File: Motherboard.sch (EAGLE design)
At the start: 8 parts

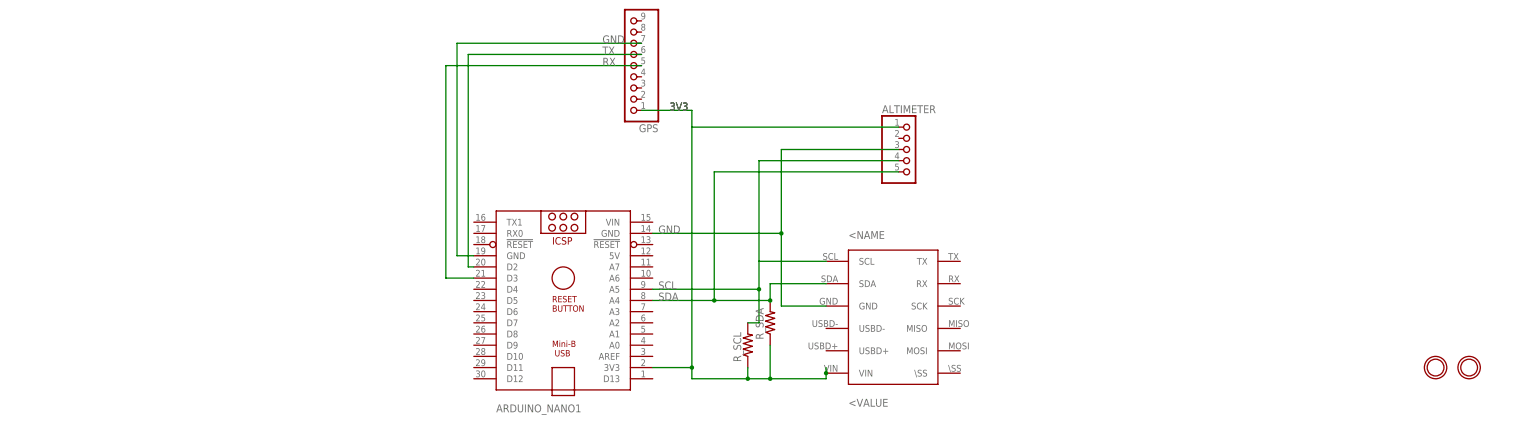
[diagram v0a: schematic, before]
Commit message: add buck converter
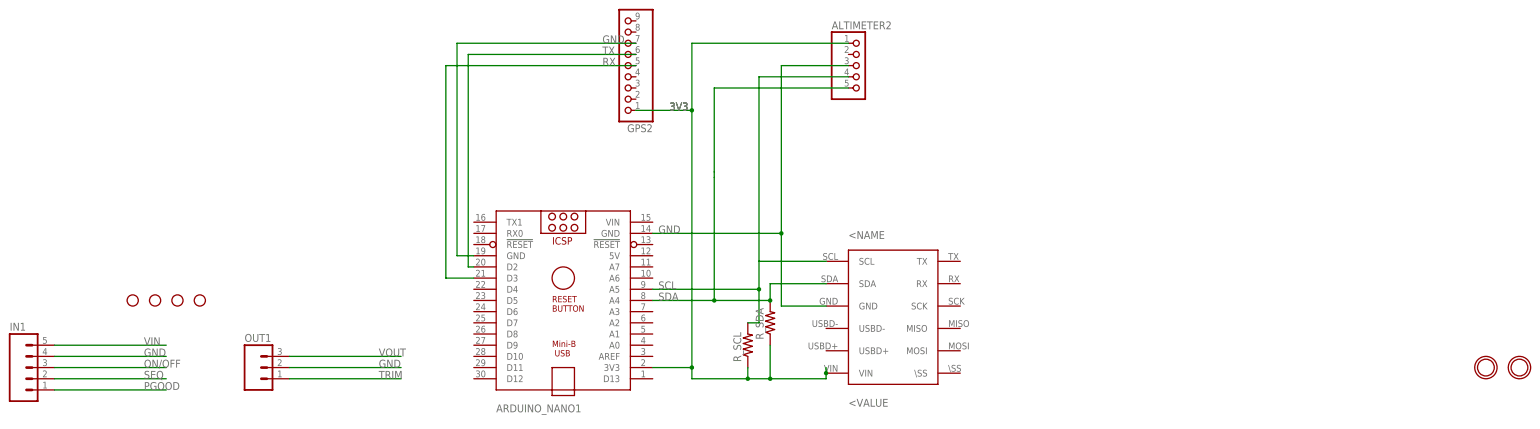
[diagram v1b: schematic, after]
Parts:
- removed ALTIMETER: (no value), microbuilder:HEADER-1X570MIL
- removed GPS: (no value), microbuilder:HEADER-1X970MIL
- added ALTIMETER2: (no value), microbuilder:HEADER-1X570MIL
- added GPS2: (no value), microbuilder:HEADER-1X970MIL
- added IN1: (no value), SparkFun:M05PTH
- added OUT1: (no value), SparkFun:M03PTH
- added U$10, U$7: STAND-OFF, SparkFun:STAND-OFF
- added U$3, U$4: MOUNTINGHOLE2.5, microbuilder:MOUNTINGHOLE2.5
- U$8, U$9: value MOUNTINGHOLE2.5 -> STAND-OFF; device microbuilder:MOUNTINGHOLE2.5 -> SparkFun:STAND-OFF
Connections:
- new net ON/OFF: IN1.3
- new net PGOOD: IN1.1
- new net SEQ: IN1.2
- new net TRIM: OUT1.1
- new net VIN: IN1.5
- new net VOUT: OUT1.3
- net 3V3: now also ALTIMETER2.1, GPS2.1; no longer ALTIMETER.1, GPS.1
- net GND: now also ALTIMETER2.3, GPS2.7, IN1.4, OUT1.2; no longer ALTIMETER.3, GPS.7
- net RX: now also GPS2.5; no longer GPS.5
- net SCL: now also ALTIMETER2.4; no longer ALTIMETER.4
- net SDA: now also ALTIMETER2.5; no longer ALTIMETER.5
- net TX: now also GPS2.6; no longer GPS.6

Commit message: test
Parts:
- added R_TRIM: (no value), rcl:R-US_R0603
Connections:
- removed net VOUT: OUT1.3
- new net GND_BATT: IN1.4
- new net V_BATT: IN1.5
- net GND: now also R_TRIM.1; no longer IN1.4
- net TRIM: now also R_TRIM.2
- net VIN: now also OUT1.3; no longer IN1.5
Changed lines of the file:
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@@
 <part name="U$9" library="SparkFun" deviceset="STAND-OFF" device=""/>
 <part name="U$10" library="SparkFun" deviceset="STAND-OFF" device=""/>
+<part name="R_TRIM" library="rcl" library_urn="urn:adsk.eagle:library:334" deviceset="R-US_" device="R0603" package3d_urn="urn:adsk.eagle:package:23555/2"/>
 </parts>
 <sheets>
@@
 <instance part="U$9" gate="G$1" x="-38.1" y="68.58"/>
 <instance part="U$10" gate="G$1" x="-43.18" y="68.58"/>
+<instance part="R_TRIM" gate="G$1" x="22.86" y="45.72" rot="R180">
+<attribute name="NAME" x="26.67" y="44.2214" size="1.778" layer="95" rot="R180"/>
+<attribute name="VALUE" x="26.67" y="49.022" size="1.778" layer="96" rot="R180"/>
+</instance>
 </instances>
 <busses>
@@
 </segment>
 <segment>
-<wire x1="-60.96" y1="55.88" x2="-35.56" y2="55.88" width="0.1524" layer="91"/>
-<label x="-40.64" y="55.88" size="1.778" layer="95"/>
-<pinref part="IN1" gate="G$1" pin="4"/>
-</segment>
-<segment>
-<wire x1="-7.62" y1="53.34" x2="17.78" y2="53.34" width="0.1524" layer="91"/>
+<wire x1="-7.62" y1="53.34" x2="27.94" y2="53.34" width="0.1524" layer="91"/>
 <label x="12.7" y="53.34" size="1.778" layer="95"/>
 <pinref part="OUT1" gate="G$1" pin="2"/>
+<pinref part="R_TRIM" gate="G$1" pin="1"/>
+<wire x1="27.94" y1="53.34" x2="27.94" y2="45.72" width="0.1524" layer="91"/>
 </segment>
 </net>
@@
 <label x="12.7" y="50.8" size="1.778" layer="95"/>
 <pinref part="OUT1" gate="G$1" pin="1"/>
+<pinref part="R_TRIM" gate="G$1" pin="2"/>
+<wire x1="17.78" y1="50.8" x2="17.78" y2="45.72" width="0.1524" layer="91"/>
 </segment>
 </net>
@@
 <net name="VIN" class="0">
 <segment>
-<wire x1="-60.96" y1="58.42" x2="-35.56" y2="58.42" width="0.1524" layer="91"/>
-<label x="-40.64" y="58.42" size="1.778" layer="95"/>
-<pinref part="IN1" gate="G$1" pin="5"/>
-</segment>
-</net>
-<net name="VOUT" class="0">
-<segment>
 <wire x1="-7.62" y1="55.88" x2="17.78" y2="55.88" width="0.1524" layer="91"/>
 <label x="12.7" y="55.88" size="1.778" layer="95"/>
@@
 </segment>
 </net>
+<net name="V_BATT" class="0">
+<segment>
+<pinref part="IN1" gate="G$1" pin="5"/>
+<wire x1="-60.96" y1="58.42" x2="-38.1" y2="58.42" width="0.1524" layer="91"/>
+<label x="-40.64" y="58.42" size="1.778" layer="95"/>
+</segment>
+</net>
+<net name="GND_BATT" class="0">
+<segment>
+<pinref part="IN1" gate="G$1" pin="4"/>
+<wire x1="-60.96" y1="55.88" x2="-35.56" y2="55.88" width="0.1524" layer="91"/>
+<label x="-40.64" y="55.88" size="1.778" layer="95"/>
+</segment>
+</net>
